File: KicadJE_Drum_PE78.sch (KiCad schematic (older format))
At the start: 112 parts, among them J101 Snare, J102 LCymbals, J103 SCymbals, J104 Maracas, J105 Bass, J106 LBongo, J107 HBongo, J108 Claves, P101 Doepfer_Power_16pin, Q101 2N3904, Q102 2N3904, Q103 2N3904, Q104 2N3904, U101 74HC04

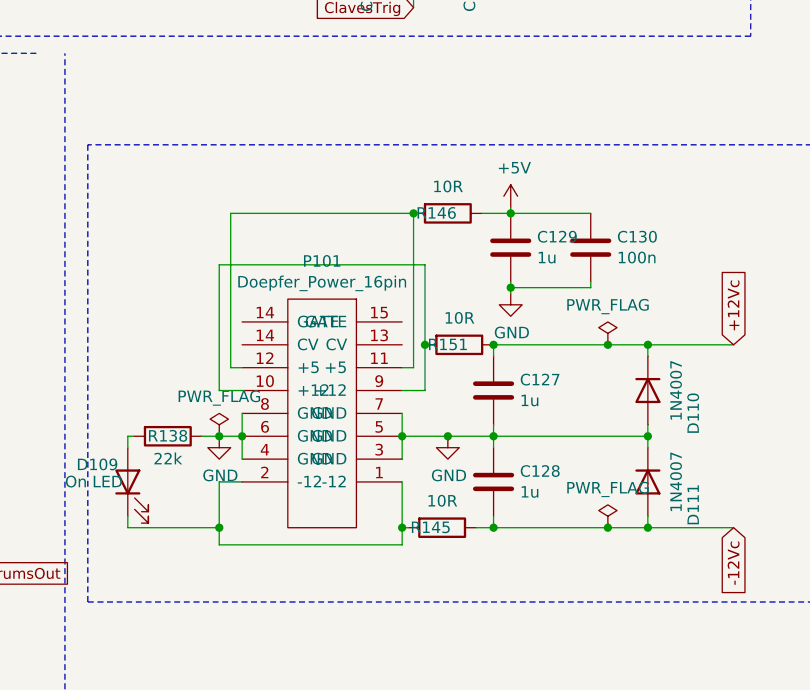
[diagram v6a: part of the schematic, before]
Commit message: ERC Performed - changed symbol for 16pin pwr
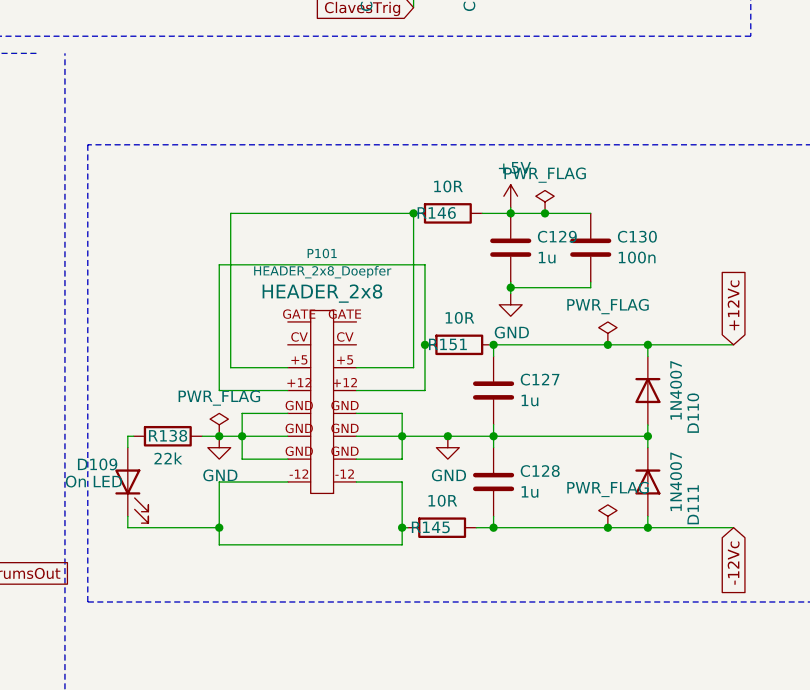
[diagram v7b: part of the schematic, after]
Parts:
- removed P101: Doepfer_Power_16pin, Connector_PinHeader_2.54mm:PinHeader_2x08_P2.54mm_Vertical, symbol Doepfer_Power_14pin:Doepfer_Power_16pin
- added P101: HEADER_2x8_Doepfer, HEADER_2x8, symbol Eurorack:HEADER_2x8_Doepfer
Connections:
- net GND: now also P101.GND (P8)
- net at D109.1 (K), R145.2: now also P101.-12 (P2)
- net at R151.2: now also P101.+12 (P9)
- net at R146.2: now also P101.+5 (P12)
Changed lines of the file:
@@
 Wire Wire Line
 	7575 5975 7575 6175
-Wire Wire Line
-	7675 5975 7575 5975
-Wire Wire Line
-	7675 5575 7575 5575
 $Comp
 L power:GND #PWR0113
@@
 Wire Wire Line
 	4800 6475 4875 6475
-$Comp
-L Doepfer_Power_14pin:Doepfer_Power_16pin P101
-U 1 1 61739A83
-P 8025 5675
-F 0 "P101" H 8025 5010 50  0000 C CNN
-F 1 "Doepfer_Power_16pin" H 8025 5101 50  0000 C CNN
-F 2 "Connector_PinHeader_2.54mm:PinHeader_2x08_P2.54mm_Vertical" H 8025 5675 50  0001 C CNN
-F 3 "DOCUMENTATION" H 8025 5675 50  0001 C CNN
-	1    8025 5675
-	-1   0    0    1
-$EndComp
 Connection ~ 8775 5375
 Wire Wire Line
@@
 Connection ~ 7575 6175
 Connection ~ 8375 6175
-Wire Wire Line
-	8375 5575 8475 5575
 Wire Wire Line
 	8475 5575 8475 5375
@@
 $EndComp
 Wire Wire Line
-	7675 5475 7625 5475
-Wire Wire Line
 	7625 5475 7625 4800
-Wire Wire Line
-	8375 5475 8425 5475
 Wire Wire Line
 	8425 4800 8425 5475
@@
 $EndComp
 Wire Wire Line
-	8850 4800 9200 4800
+	8850 4800 9000 4800
 Wire Wire Line
 	9200 5100 9200 5125
@@
 Wire Wire Line
 	8850 5125 8850 5100
+$Comp
+L Eurorack:HEADER_2x8_Doepfer P101
+U 1 1 6082CE5A
+P 8025 5675
+F 0 "P101" H 8025 4977 40  0000 C CNN
+F 1 "HEADER_2x8_Doepfer" H 8025 5053 40  0000 C CNN
+F 2 "HEADER_2x8" H 8025 5144 60  0000 C CNN
+F 3 "" H 8025 5675 60  0000 C CNN
+	1    8025 5675
+	-1   0    0    1
+$EndComp
+Wire Wire Line
+	7625 5475 7875 5475
+Wire Wire Line
+	7575 5575 7875 5575
+Wire Wire Line
+	7675 5675 7875 5675
+Wire Wire Line
+	7675 5875 7875 5875
+Wire Wire Line
+	7875 5775 7675 5775
+Wire Wire Line
+	7575 5975 7875 5975
+Wire Wire Line
+	8175 5975 8375 5975
+Wire Wire Line
+	8375 5875 8175 5875
+Wire Wire Line
+	8375 5675 8175 5675
+Wire Wire Line
+	8175 5775 8375 5775
+Wire Wire Line
+	8175 5575 8475 5575
+Wire Wire Line
+	8175 5475 8425 5475
+$Comp
+L power:PWR_FLAG #FLG0104
+U 1 1 609C6001
+P 9000 4800
+F 0 "#FLG0104" H 9000 4875 50  0001 C CNN
+F 1 "PWR_FLAG" H 9000 4973 50  0000 C CNN
+F 2 "" H 9000 4800 50  0001 C CNN
+F 3 "~" H 9000 4800 50  0001 C CNN
+	1    9000 4800
+	1    0    0    -1
+$EndComp
+Connection ~ 9000 4800
+Wire Wire Line
+	9000 4800 9200 4800
 $EndSCHEMATC

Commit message: Footprint adj
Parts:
- RV101: footprint (none) -> Potentiometer_THT:Potentiometer_Bourns_3296W_Vertical
- U101: footprint (none) -> AJ:AJ_SO-14_5.3x6.2mm_P1.27mm
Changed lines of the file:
@@
 F 0 "U101" H 3875 1042 50  0000 C CNN
 F 1 "74HC04" H 3875 951 50  0000 C CNN
-F 2 "" H 3875 725 50  0001 C CNN
+F 2 "AJ:AJ_SO-14_5.3x6.2mm_P1.27mm" H 3875 725 50  0001 C CNN
 F 3 "https://assets.nexperia.com/documents/data-sheet/74HC_HCT04.pdf" H 3875 725 50  0001 C CNN
 	1    3875 725
@@
 F 0 "U101" H 8500 1042 50  0000 C CNN
 F 1 "74HC04" H 8500 951 50  0000 C CNN
-F 2 "" H 8500 725 50  0001 C CNN
+F 2 "AJ:AJ_SO-14_5.3x6.2mm_P1.27mm" H 8500 725 50  0001 C CNN
 F 3 "https://assets.nexperia.com/documents/data-sheet/74HC_HCT04.pdf" H 8500 725 50  0001 C CNN
 	2    8500 725
@@
 F 0 "U101" H 3875 2867 50  0000 C CNN
 F 1 "74HC04" H 3875 2776 50  0000 C CNN
-F 2 "" H 3875 2550 50  0001 C CNN
+F 2 "AJ:AJ_SO-14_5.3x6.2mm_P1.27mm" H 3875 2550 50  0001 C CNN
 F 3 "https://assets.nexperia.com/documents/data-sheet/74HC_HCT04.pdf" H 3875 2550 50  0001 C CNN
 	3    3875 2550
@@
 F 0 "U101" H 8450 2842 50  0000 C CNN
 F 1 "74HC04" H 8450 2751 50  0000 C CNN
-F 2 "" H 8450 2525 50  0001 C CNN
+F 2 "AJ:AJ_SO-14_5.3x6.2mm_P1.27mm" H 8450 2525 50  0001 C CNN
 F 3 "https://assets.nexperia.com/documents/data-sheet/74HC_HCT04.pdf" H 8450 2525 50  0001 C CNN
 	4    8450 2525
@@
 F 0 "U101" H 10905 5621 50  0000 L CNN
 F 1 "74HC04" H 10905 5530 50  0000 L CNN
-F 2 "" H 10675 5575 50  0001 C CNN
+F 2 "AJ:AJ_SO-14_5.3x6.2mm_P1.27mm" H 10675 5575 50  0001 C CNN
 F 3 "https://assets.nexperia.com/documents/data-sheet/74HC_HCT04.pdf" H 10675 5575 50  0001 C CNN
 	7    10675 5575
@@
 F 0 "RV101" V 3593 5100 50  0000 C CNN
 F 1 "R_POT_TRIM" V 3684 5100 50  0000 C CNN
-F 2 "" H 3800 5100 50  0001 C CNN
+F 2 "Potentiometer_THT:Potentiometer_Bourns_3296W_Vertical" H 3800 5100 50  0001 C CNN
 F 3 "~" H 3800 5100 50  0001 C CNN
 	1    3800 5100
